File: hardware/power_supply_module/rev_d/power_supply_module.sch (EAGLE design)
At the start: 166 parts, among them J1 MODULE_POWER, J3 TC2030-CTX-NL, Q1 MOSFET-NCHANNELFDD8580, U1 TLV62130, U10 LTC2943, U11 LTC2943, U12 LTC2943, U13 LTC2943, U14 LTC2943, U15 LTC2943, U16 LT3652, U17 LM234, U18 MAX17205, U19 ESDR0502N, U2 TLV62130, U20 AP22814, U21 AP22814, U22 AP22814, U23 AP22814, U24 AP22814, U25 PCA9544AQFN-N20, U26 LTC2943, U27 MAX6746, U28 3.3V, U29 M24C01WMN, U3 TLV62130, U4 TLV62130, U5 TLV62130, U6 PCA9544AQFN-N20, U7 PCA9544AQFN-N20, U8 LTC2943, U9 LTC2943

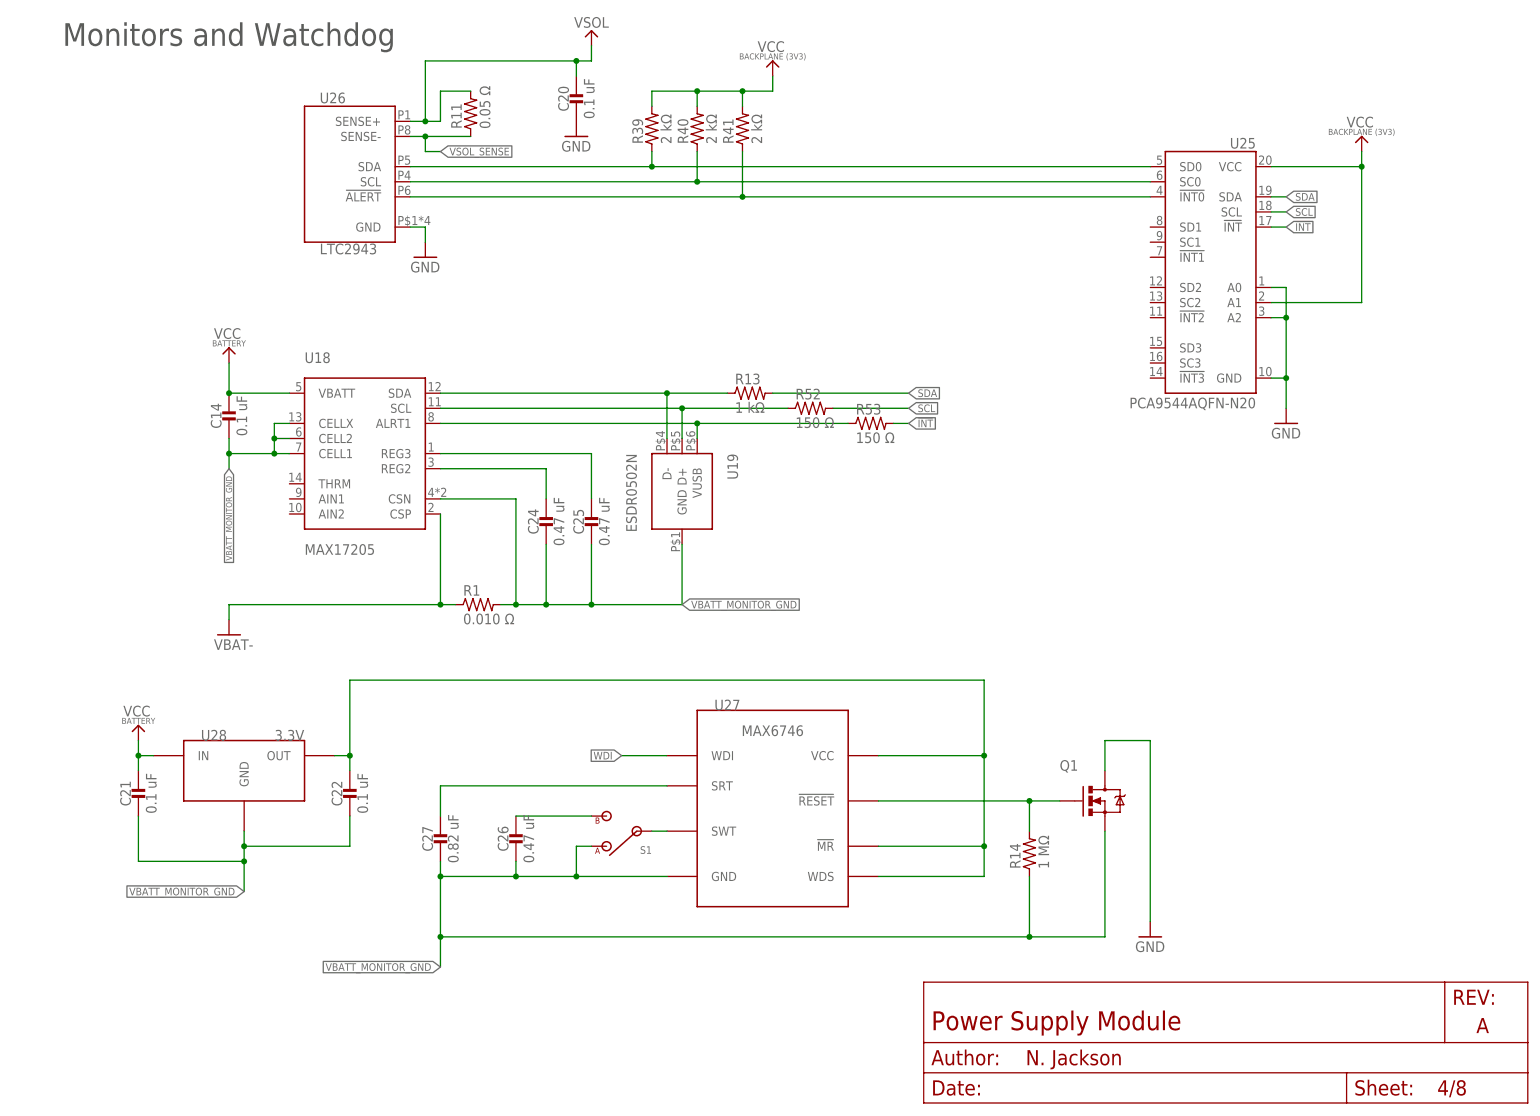
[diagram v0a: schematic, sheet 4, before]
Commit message: almost all changes made - need to check over resistor values
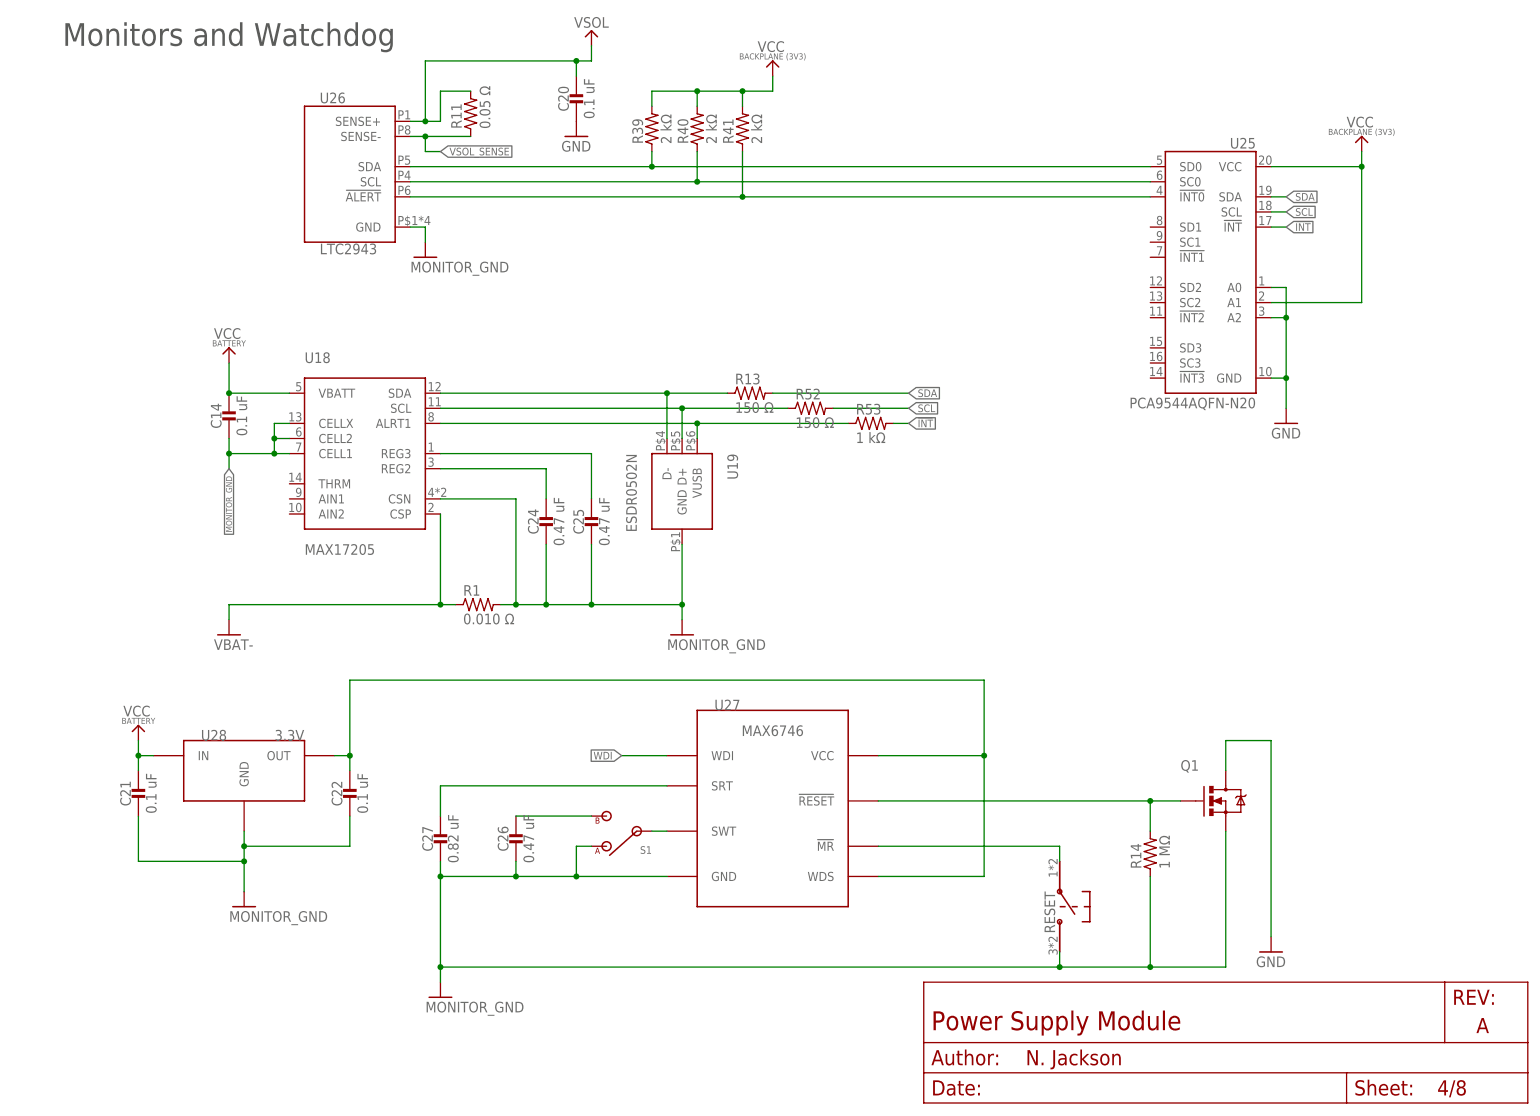
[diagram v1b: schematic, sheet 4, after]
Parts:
- added RESET: PTS810SJ, switches:PTS810SJ
- D3: value DIODE_SCHOTTKYSOT-23F -> DIODE_SCHOTTKYSOD323; device passives:DIODE_SCHOTTKYSOT-23F -> passives:DIODE_SCHOTTKYSOD323
- R13: value 1 kΩ -> 150 Ω
- R42, R55, R56, R62: device passives:RESISTOR0402_RES -> passives:RESISTOR0805_RES
- R53: value 150 Ω -> 1 kΩ
- U8: value LTC2943 -> LTC2941; device chips:LTC2943 -> chips:LTC2941
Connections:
- removed net VBATT_MONITOR_GND: C14.2, C21.2, C22.2, C24.2, C25.2, C26.2, C27.2, Q1.S, R1.2, R14.1, S1.A, U18.CELL1, U18.CELL2, U18.CELLX, U18.CSN, U19.GND, U27.GND, U28.GND, VBATT-M.TESTPOINT
- new net MONITOR_GND: C14.2, C21.2, C22.2, C24.2, C25.2, C26.2, C27.2, C39.2, C40.2, D1.ANODE, J1.VSOL-, Q1.S, R1.2, R14.1, R42.1, R56.2, RESET.P$2, S1.A, U16.GND, U16.TIMER, U18.CELL1, U18.CELL2, U18.CELLX, U18.CSN, U19.GND, U26.GND, U27.GND, U28.GND, VBATT-M.TESTPOINT
- new net N$20: RESET.P$1, U27.!MR
- net GND: no longer C39.2, C40.2, D1.ANODE, J1.VSOL-, R42.1, R56.2, U16.GND, U16.TIMER, U26.GND
- net N$72: no longer U27.!MR
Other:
- moved on the sheet: D1, Q1, R14, U8

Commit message: change to .01% voltage divider resistors
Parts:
- R42: DIGIKEY 311-2257-1-ND -> P23.2KDATR-ND
- R55: DIGIKEY P301KLCT-ND -> P301KDATR-ND
- R56: DIGIKEY P340KLCT-ND -> P340KDACT-ND
- R62: DIGIKEY P953KLCT-ND -> P953KDACT-ND
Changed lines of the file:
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@@
 <grid distance="0.1" unitdist="inch" unit="inch" style="lines" multiple="1" display="no" altdistance="0.01" altunitdist="inch" altunit="inch"/>
 <layers>
-<layer number="1" name="Top" color="4" fill="1" visible="yes" active="no"/>
-<layer number="2" name="Route2" color="12" fill="4" visible="yes" active="no"/>
-<layer number="3" name="Route3" color="4" fill="3" visible="yes" active="no"/>
-<layer number="4" name="Route4" color="1" fill="4" visible="yes" active="no"/>
-<layer number="5" name="Route5" color="4" fill="4" visible="yes" active="no"/>
-<layer number="6" name="Route6" color="1" fill="8" visible="yes" active="no"/>
-<layer number="7" name="Route7" color="4" fill="8" visible="yes" active="no"/>
-<layer number="8" name="Route8" color="1" fill="2" visible="yes" active="no"/>
-<layer number="9" name="Route9" color="4" fill="2" visible="yes" active="no"/>
-<layer number="10" name="Route10" color="1" fill="7" visible="yes" active="no"/>
-<layer number="11" name="Route11" color="4" fill="7" visible="yes" active="no"/>
-<layer number="12" name="Route12" color="1" fill="5" visible="yes" active="no"/>
-<layer number="13" name="Route13" color="4" fill="5" visible="yes" active="no"/>
-<layer number="14" name="Route14" color="1" fill="6" visible="yes" active="no"/>
-<layer number="15" name="Route15" color="9" fill="5" visible="yes" active="no"/>
-<layer number="16" name="Bottom" color="1" fill="1" visible="yes" active="no"/>
-<layer number="17" name="Pads" color="2" fill="1" visible="yes" active="no"/>
-<layer number="18" name="Vias" color="2" fill="1" visible="yes" active="no"/>
-<layer number="19" name="Unrouted" color="6" fill="1" visible="yes" active="no"/>
-<layer number="20" name="Dimension" color="15" fill="1" visible="yes" active="no"/>
-<layer number="21" name="tPlace" color="7" fill="1" visible="yes" active="no"/>
-<layer number="22" name="bPlace" color="7" fill="1" visible="yes" active="no"/>
-<layer number="23" name="tOrigins" color="15" fill="1" visible="yes" active="no"/>
-<layer number="24" name="bOrigins" color="15" fill="1" visible="yes" active="no"/>
-<layer number="25" name="tNames" color="7" fill="1" visible="yes" active="no"/>
-<layer number="26" name="bNames" color="7" fill="1" visible="yes" active="no"/>
-<layer number="27" name="tValues" color="7" fill="1" visible="yes" active="no"/>
-<layer number="28" name="bValues" color="7" fill="1" visible="yes" active="no"/>
+<layer number="1" name="Top" color="4" fill="1" visible="no" active="no"/>
+<layer number="2" name="Route2" color="12" fill="4" visible="no" active="no"/>
+<layer number="3" name="Route3" color="4" fill="3" visible="no" active="no"/>
+<layer number="4" name="Route4" color="1" fill="4" visible="no" active="no"/>
+<layer number="5" name="Route5" color="4" fill="4" visible="no" active="no"/>
+<layer number="6" name="Route6" color="1" fill="8" visible="no" active="no"/>
+<layer number="7" name="Route7" color="4" fill="8" visible="no" active="no"/>
+<layer number="8" name="Route8" color="1" fill="2" visible="no" active="no"/>
+<layer number="9" name="Route9" color="4" fill="2" visible="no" active="no"/>
+<layer number="10" name="Route10" color="1" fill="7" visible="no" active="no"/>
+<layer number="11" name="Route11" color="4" fill="7" visible="no" active="no"/>
+<layer number="12" name="Route12" color="1" fill="5" visible="no" active="no"/>
+<layer number="13" name="Route13" color="4" fill="5" visible="no" active="no"/>
+<layer number="14" name="Route14" color="1" fill="6" visible="no" active="no"/>
+<layer number="15" name="Route15" color="9" fill="5" visible="no" active="no"/>
+<layer number="16" name="Bottom" color="1" fill="1" visible="no" active="no"/>
+<layer number="17" name="Pads" color="2" fill="1" visible="no" active="no"/>
+<layer number="18" name="Vias" color="2" fill="1" visible="no" active="no"/>
+<layer number="19" name="Unrouted" color="6" fill="1" visible="no" active="no"/>
+<layer number="20" name="Dimension" color="15" fill="1" visible="no" active="no"/>
+<layer number="21" name="tPlace" color="7" fill="1" visible="no" active="no"/>
+<layer number="22" name="bPlace" color="7" fill="1" visible="no" active="no"/>
+<layer number="23" name="tOrigins" color="15" fill="1" visible="no" active="no"/>
+<layer number="24" name="bOrigins" color="15" fill="1" visible="no" active="no"/>
+<layer number="25" name="tNames" color="7" fill="1" visible="no" active="no"/>
+<layer number="26" name="bNames" color="7" fill="1" visible="no" active="no"/>
+<layer number="27" name="tValues" color="7" fill="1" visible="no" active="no"/>
+<layer number="28" name="bValues" color="7" fill="1" visible="no" active="no"/>
 <layer number="29" name="tStop" color="7" fill="3" visible="no" active="no"/>
 <layer number="30" name="bStop" color="7" fill="6" visible="no" active="no"/>
@@
 <layer number="35" name="tGlue" color="7" fill="4" visible="no" active="no"/>
 <layer number="36" name="bGlue" color="7" fill="5" visible="no" active="no"/>
-<layer number="37" name="tTest" color="7" fill="1" visible="yes" active="no"/>
-<layer number="38" name="bTest" color="7" fill="1" visible="yes" active="no"/>
+<layer number="37" name="tTest" color="7" fill="1" visible="no" active="no"/>
+<layer number="38" name="bTest" color="7" fill="1" visible="no" active="no"/>
 <layer number="39" name="tKeepout" color="4" fill="11" visible="no" active="no"/>
 <layer number="40" name="bKeepout" color="1" fill="11" visible="no" active="no"/>
@@
 <layer number="44" name="Drills" color="7" fill="1" visible="no" active="no"/>
 <layer number="45" name="Holes" color="7" fill="1" visible="no" active="no"/>
-<layer number="46" name="Milling" color="3" fill="1" visible="yes" active="no"/>
-<layer number="47" name="Measures" color="7" fill="1" visible="yes" active="no"/>
-<layer number="48" name="Document" color="7" fill="1" visible="yes" active="no"/>
-<layer number="49" name="Reference" color="7" fill="1" visible="yes" active="no"/>
-<layer number="50" name="dxf" color="7" fill="1" visible="yes" active="no"/>
-<layer number="51" name="tDocu" color="7" fill="1" visible="yes" active="no"/>
-<layer number="52" name="bDocu" color="7" fill="1" visible="yes" active="no"/>
-<layer number="53" name="tGND_GNDA" color="7" fill="9" visible="yes" active="no"/>
-<layer number="54" name="bGND_GNDA" color="1" fill="9" visible="yes" active="no"/>
-<layer number="56" name="wert" color="7" fill="1" visible="yes" active="no"/>
-<layer number="57" name="tCAD" color="7" fill="1" visible="yes" active="no"/>
-<layer number="59" name="Invisible" color="7" fill="1" visible="yes" active="no"/>
-<layer number="60" name="bCarbon" color="7" fill="1" visible="yes" active="no"/>
-<layer number="61" name="stand" color="7" fill="1" visible="yes" active="no"/>
+<layer number="46" name="Milling" color="3" fill="1" visible="no" active="no"/>
+<layer number="47" name="Measures" color="7" fill="1" visible="no" active="no"/>
+<layer number="48" name="Document" color="7" fill="1" visible="no" active="no"/>
+<layer number="49" name="Reference" color="7" fill="1" visible="no" active="no"/>
+<layer number="50" name="dxf" color="7" fill="1" visible="no" active="no"/>
+<layer number="51" name="tDocu" color="7" fill="1" visible="no" active="no"/>
+<layer number="52" name="bDocu" color="7" fill="1" visible="no" active="no"/>
+<layer number="53" name="tGND_GNDA" color="7" fill="9" visible="no" active="no"/>
+<layer number="54" name="bGND_GNDA" color="1" fill="9" visible="no" active="no"/>
+<layer number="56" name="wert" color="7" fill="1" visible="no" active="no"/>
+<layer number="57" name="tCAD" color="7" fill="1" visible="no" active="no"/>
+<layer number="59" name="Invisible" color="7" fill="1" visible="no" active="no"/>
+<layer number="60" name="bCarbon" color="7" fill="1" visible="no" active="no"/>
+<layer number="61" name="stand" color="7" fill="1" visible="no" active="no"/>
 <layer number="90" name="Modules" color="5" fill="1" visible="yes" active="yes"/>
 <layer number="91" name="Nets" color="2" fill="1" visible="yes" active="yes"/>
@@
 </part>
 <part name="R62" library="passives" deviceset="RESISTOR" device="0805_RES" value="953 kΩ">
-<attribute name="DIGIKEY" value="P953KLCT-ND"/>
+<attribute name="DIGIKEY" value="P953KDACT-ND"/>
 </part>
 <part name="R56" library="passives" deviceset="RESISTOR" device="0805_RES" value="340 kΩ">
-<attribute name="DIGIKEY" value="P340KLCT-ND"/>
+<attribute name="DIGIKEY" value="P340KDACT-ND"/>
 </part>
 <part name="U17" library="chips" deviceset="LM234" device=""/>
@@
 </part>
 <part name="R55" library="passives" deviceset="RESISTOR" device="0805_RES" value="301 kΩ">
-<attribute name="DIGIKEY" value="P301KLCT-ND"/>
+<attribute name="DIGIKEY" value="P301KDATR-ND"/>
 </part>
 <part name="R42" library="passives" deviceset="RESISTOR" device="0805_RES" value="23.2 kΩ">
-<attribute name="DIGIKEY" value="311-2257-1-ND"/>
+<attribute name="DIGIKEY" value="P23.2KDATR-ND"/>
 </part>
 <part name="C40" library="passives" deviceset="CAPACITOR" device="0805_CAP" value="10 uF">

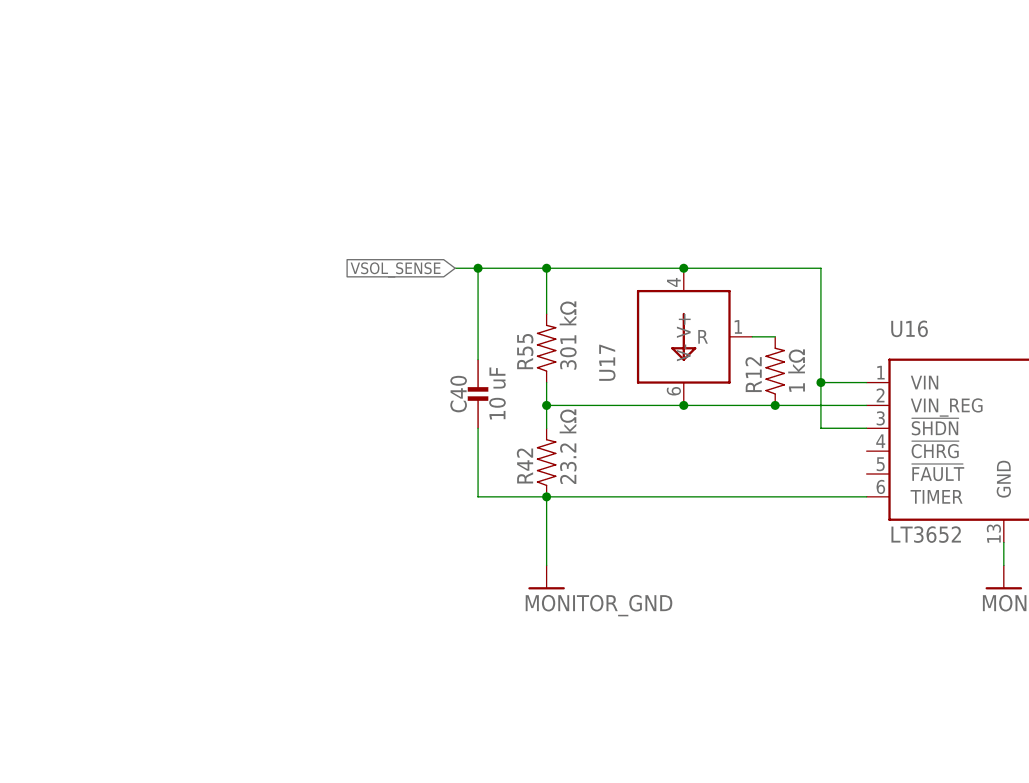
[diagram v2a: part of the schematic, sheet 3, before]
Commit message: reroute charger
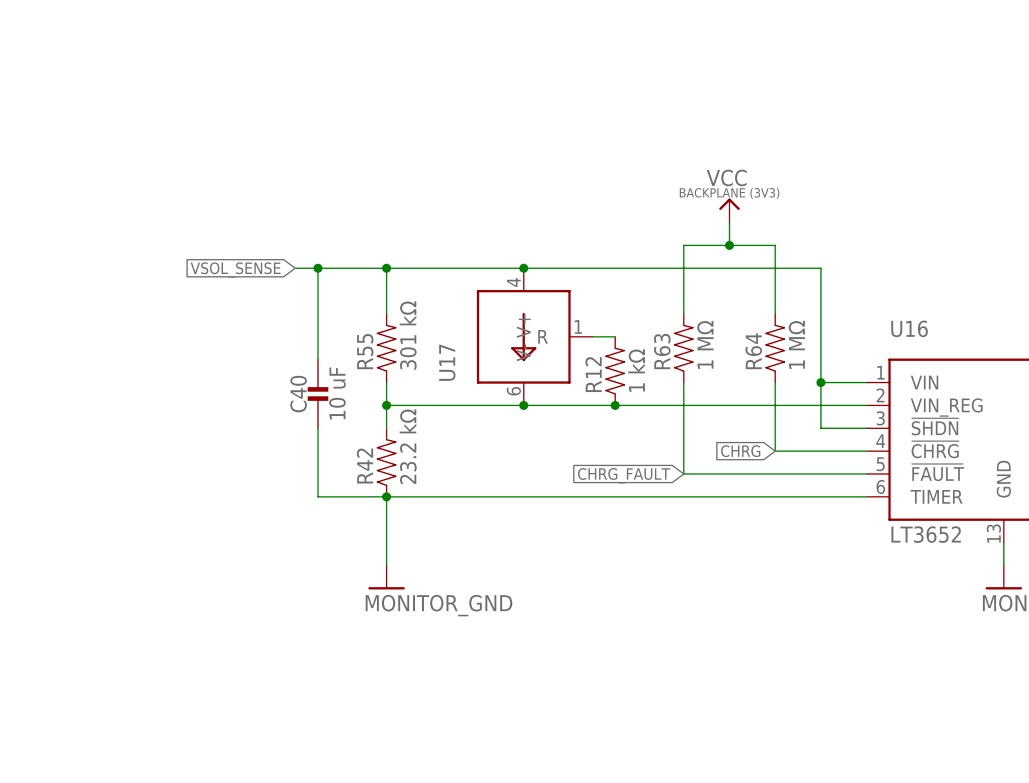
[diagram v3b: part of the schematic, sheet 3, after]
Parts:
- added CHRG, CHRG_FAULT: TEST_POINT_0.040IN, headers:TEST_POINT_0.040IN
- added R63, R64: 1 MΩ, passives:RESISTOR0402_RES
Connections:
- new net CHRG: CHRG.TESTPOINT, R64.1, U16.!CHRG
- new net CHRG_FAULT: CHRG_FAULT.TESTPOINT, R63.1, U16.!FAULT
- net VCC_BACKPLANE: now also R63.2, R64.2
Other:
- moved on the sheet: 3V3, 5V_1, 5V_2, 5V_3, 5V_4, C40, R12, R42, R55, U17, VBATT-M
